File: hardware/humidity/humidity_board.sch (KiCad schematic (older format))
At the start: 11 parts

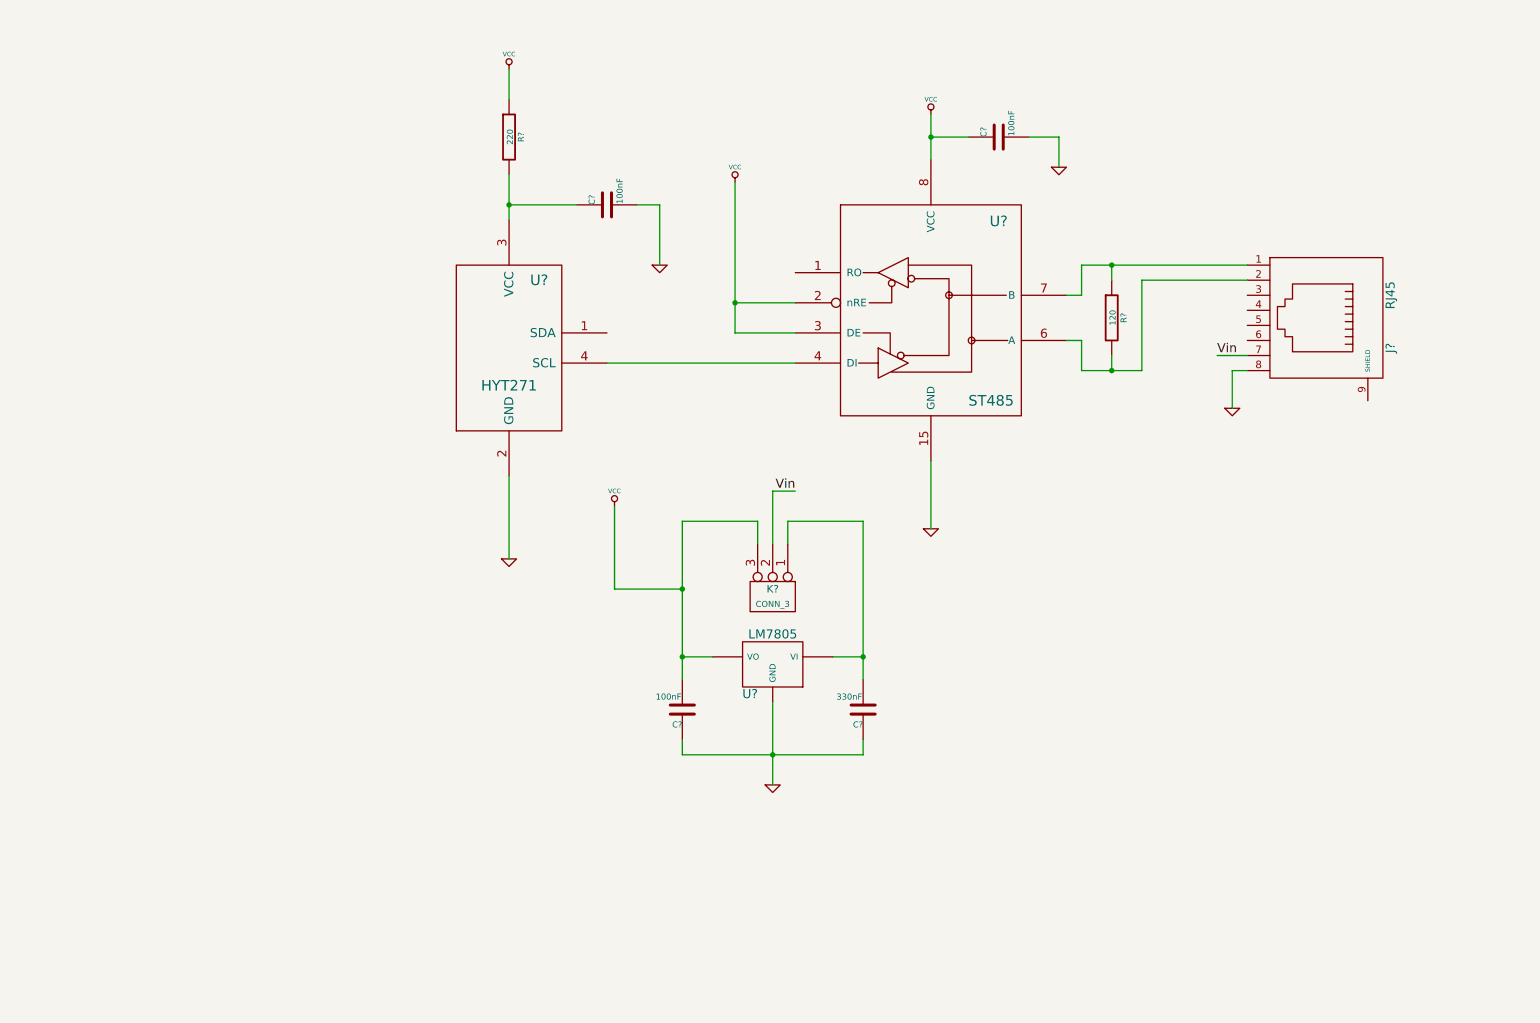
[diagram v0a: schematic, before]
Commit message: complete humidity board schematic
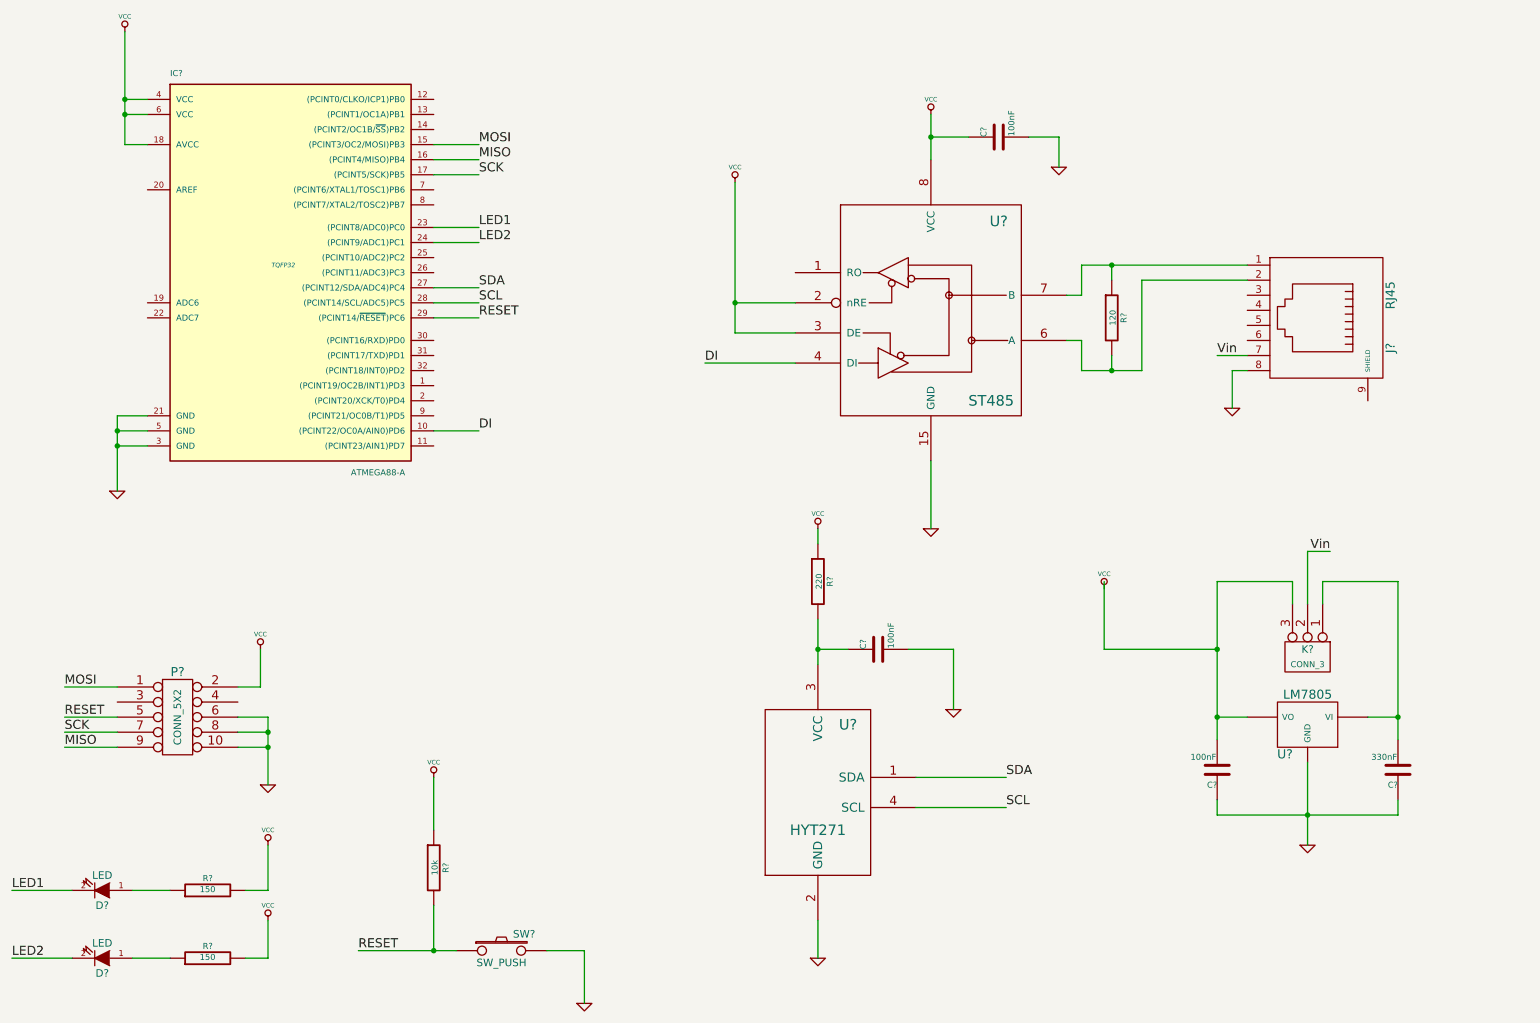
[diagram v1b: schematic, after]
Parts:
- added D? (x2): LED, ~, symbol LED
- added IC?: ATMEGA88-A, TQFP32, symbol ATMEGA88-A
- added P?: CONN_5X2, ~, symbol CONN_5X2
- added R?: 10k, ~, symbol R
- added R? (x2): 150, ~, symbol R
- added SW?: SW_PUSH, ~, symbol SW_PUSH
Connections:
- net GND: now also IC?.21 (GND), IC?.3 (GND), IC?.5 (GND), P?.10, P?.6, P?.8, SW?.2
- net VCC: now also IC?.18 (AVCC), IC?.4 (VCC), IC?.6 (VCC), P?.2, R?.1, R?.2, R?.2; no longer C?.2, K?.3 (P3), U?.VO
- net DI: now reaches U?.4 (DI)
- net DI: now also IC?.10 ((PCINT22/OC0A/AIN0)PD6); no longer U?.4 (SCL)
- net SDA: now reaches U?.1 (SDA)
- net SDA: now also IC?.27 ((PCINT12/SDA/ADC4)PC4)
- new net: C?.2, K?.3 (P3), U?.VO
- new net: D?.1 (A), R?.1 (x2)
- new net LED1: D?.2 (K), IC?.23 ((PCINT8/ADC0)PC0)
- new net LED2: D?.2 (K), IC?.24 ((PCINT9/ADC1)PC1)
- new net MISO: IC?.16 ((PCINT4/MISO)PB4), P?.9
- new net MOSI: IC?.15 ((PCINT3/OC2/MOSI)PB3), P?.1
- new net RESET: IC?.29 ((PCINT14/~RESET~)PC6), P?.5, R?.2, SW?.1
- new net SCK: IC?.17 ((PCINT5/SCK)PB5), P?.7
- new net SCL: IC?.28 ((PCINT14/SCL/ADC5)PC5), U?.4 (SCL)
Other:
- moved on the sheet: C?, K?, R?, U?

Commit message: hardware + bestellungen
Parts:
- removed C?: 100nF, ~, symbol C
- removed C?: 330nF, ~, symbol C
- removed K?: CONN_3, ~, symbol CONN_3
- removed U?: LM7805, ~, symbol LM7805
- added C?: 100nF, ~, symbol C
- added R? (x2): 22k, ~, symbol R
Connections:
- net Vin is gone; now on net VCC: J?.7
- net GND: now also J?.9 (SHIELD), R?.2
- net VCC: now also R?.1
- net at J?.2, U?.6 (A): now also C?.1, R?.2; no longer R?.2
- net at J?.1, R?.1, U?.7 (B): now also R?.1
- new net: C?.2, R?.2
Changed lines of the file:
@@
 LIBS:TSic50xF
 LIBS:ST485
-LIBS:HYT271
 LIBS:humidity_board-cache
 EELAYER 27 0
@@
 Sheet 1 1
 Title ""
-Date "24 mar 2014"
+Date "12 apr 2014"
 Rev ""
 Comp ""
@@
 Comment4 ""
 $EndDescr
-$Comp
-L GND #PWR?
-U 1 1 532DBFDE
-P 9300 6400
-F 0 "#PWR?" H 9300 6400 30  0001 C CNN
-F 1 "GND" H 9300 6330 30  0001 C CNN
-F 2 "" H 9300 6400 60  0000 C CNN
-F 3 "" H 9300 6400 60  0000 C CNN
-	1    9300 6400
-	1    0    0    -1
-$EndComp
 $Comp
 L VCC #PWR?
@@
 $EndComp
 $Comp
-L LM7805 U?
-U 1 1 532DDDDB
-P 9300 5600
-F 0 "U?" H 9450 5404 60  0000 C CNN
-F 1 "LM7805" H 9300 5800 60  0000 C CNN
-F 2 "~" H 9300 5600 60  0000 C CNN
-F 3 "~" H 9300 5600 60  0000 C CNN
-	1    9300 5600
-	-1   0    0    -1
-$EndComp
-$Comp
 L GND #PWR?
 U 1 1 532DDE77
@@
 	1    8800 3500
 	1    0    0    -1
-$EndComp
-$Comp
-L CONN_3 K?
-U 1 1 532DDF17
-P 9300 5150
-F 0 "K?" V 9250 5150 50  0000 C CNN
-F 1 "CONN_3" V 9350 5150 40  0000 C CNN
-F 2 "~" H 9300 5150 60  0000 C CNN
-F 3 "~" H 9300 5150 60  0000 C CNN
-	1    9300 5150
-	0    1    1    0
-$EndComp
-Text Label 9450 4450 2    60   ~ 0
-Vin
-Text Label 8700 3150 0    60   ~ 0
-Vin
-$Comp
-L VCC #PWR?
-U 1 1 532DE001
-P 7950 4700
-F 0 "#PWR?" H 7950 4800 30  0001 C CNN
-F 1 "VCC" H 7950 4800 30  0000 C CNN
-F 2 "" H 7950 4700 60  0000 C CNN
-F 3 "" H 7950 4700 60  0000 C CNN
-	1    7950 4700
-	1    0    0    -1
-$EndComp
-$Comp
-L C C?
-U 1 1 532DE060
-P 8700 5900
-F 0 "C?" H 8700 6000 40  0000 L CNN
-F 1 "100nF" H 8706 5815 40  0000 L CNN
-F 2 "~" H 8738 5750 30  0000 C CNN
-F 3 "~" H 8700 5900 60  0000 C CNN
-	1    8700 5900
-	-1   0    0    1
-$EndComp
-$Comp
-L C C?
-U 1 1 532DE066
-P 9900 5900
-F 0 "C?" H 9900 6000 40  0000 L CNN
-F 1 "330nF" H 9906 5815 40  0000 L CNN
-F 2 "~" H 9938 5750 30  0000 C CNN
-F 3 "~" H 9900 5900 60  0000 C CNN
-	1    9900 5900
-	-1   0    0    1
 $EndComp
 $Comp
@@
 	7700 3050 7800 3050
 Wire Wire Line
-	7800 3050 7800 3250
-Wire Wire Line
-	7800 3250 8200 3250
-Wire Wire Line
-	8000 3250 8000 3150
+	7800 3050 7800 3800
 Wire Wire Line
 	7800 2750 7800 2550
@@
 	8800 3250 8800 3500
 Wire Wire Line
-	9400 4800 9400 4650
-Wire Wire Line
-	9400 4650 9900 4650
-Wire Wire Line
-	9900 4650 9900 5700
-Wire Wire Line
-	9900 5550 9700 5550
-Wire Wire Line
-	9200 4800 9200 4650
-Wire Wire Line
-	9200 4650 8700 4650
-Wire Wire Line
-	8700 4650 8700 5700
-Wire Wire Line
-	8700 5550 8900 5550
-Wire Wire Line
-	9300 4800 9300 4450
-Wire Wire Line
-	9300 4450 9450 4450
-Wire Wire Line
 	8700 3150 8900 3150
-Connection ~ 8700 5100
-Wire Wire Line
-	9300 5850 9300 6400
-Connection ~ 8700 5550
-Connection ~ 9900 5550
-Wire Wire Line
-	8700 6100 8700 6200
-Wire Wire Line
-	8700 6200 9900 6200
-Connection ~ 9300 6200
-Wire Wire Line
-	9900 6200 9900 6100
 Connection ~ 8000 2550
 Wire Wire Line
 	8900 2650 8200 2650
 Wire Wire Line
-	8200 2650 8200 3250
-Connection ~ 8000 3250
+	8200 2650 8200 3800
 Wire Wire Line
 	6050 4900 6050 5200
 Wire Wire Line
 	6050 7150 6050 6900
-Wire Wire Line
-	7950 4650 7950 5100
-Wire Wire Line
-	7950 5100 8700 5100
 Wire Wire Line
 	1600 3550 1400 3550
@@
 Wire Wire Line
 	1750 7150 1500 7150
+$Comp
+L VCC #PWR?
+U 1 1 53493890
+P 8700 2950
+F 0 "#PWR?" H 8700 3050 30  0001 C CNN
+F 1 "VCC" H 8700 3050 30  0000 C CNN
+F 2 "" H 8700 2950 60  0000 C CNN
+F 3 "" H 8700 2950 60  0000 C CNN
+	1    8700 2950
+	1    0    0    -1
+$EndComp
+Wire Wire Line
+	8700 2950 8700 3150
+$Comp
+L C C?
+U 1 1 534938E9
+P 8000 3500
+F 0 "C?" H 8000 3600 40  0000 L CNN
+F 1 "100nF" H 8006 3415 40  0000 L CNN
+F 2 "~" H 8038 3350 30  0000 C CNN
+F 3 "~" H 8000 3500 60  0000 C CNN
+	1    8000 3500
+	-1   0    0    1
+$EndComp
+Wire Wire Line
+	8200 3800 7800 3800
+Wire Wire Line
+	8000 3700 8000 3800
+Connection ~ 8000 3800
+Wire Wire Line
+	8000 3150 8000 3300
+$Comp
+L R R?
+U 1 1 534939E7
+P 8350 2000
+F 0 "R?" V 8430 2000 40  0000 C CNN
+F 1 "22k" V 8357 2001 40  0000 C CNN
+F 2 "~" V 8280 2000 30  0000 C CNN
+F 3 "~" H 8350 2000 30  0000 C CNN
+	1    8350 2000
+	1    0    0    -1
+$EndComp
+$Comp
+L R R?
+U 1 1 534939ED
+P 8500 3050
+F 0 "R?" V 8580 3050 40  0000 C CNN
+F 1 "22k" V 8507 3051 40  0000 C CNN
+F 2 "~" V 8430 3050 30  0000 C CNN
+F 3 "~" H 8500 3050 30  0000 C CNN
+	1    8500 3050
+	1    0    0    -1
+$EndComp
+$Comp
+L GND #PWR?
+U 1 1 534939F3
+P 8500 3500
+F 0 "#PWR?" H 8500 3500 30  0001 C CNN
+F 1 "GND" H 8500 3430 30  0001 C CNN
+F 2 "" H 8500 3500 60  0000 C CNN
+F 3 "" H 8500 3500 60  0000 C CNN
+	1    8500 3500
+	1    0    0    -1
+$EndComp
+$Comp
+L VCC #PWR?
+U 1 1 534939F9
+P 8350 1600
+F 0 "#PWR?" H 8350 1700 30  0001 C CNN
+F 1 "VCC" H 8350 1700 30  0000 C CNN
+F 2 "" H 8350 1600 60  0000 C CNN
+F 3 "" H 8350 1600 60  0000 C CNN
+	1    8350 1600
+	1    0    0    -1
+$EndComp
+Wire Wire Line
+	8350 1600 8350 1750
+Wire Wire Line
+	8350 2250 8350 2650
+Connection ~ 8350 2650
+Wire Wire Line
+	8500 2800 8500 2550
+Connection ~ 8500 2550
+Wire Wire Line
+	8500 3300 8500 3500
+$Comp
+L GND #PWR?
+U 1 1 53493BBC
+P 9700 3600
+F 0 "#PWR?" H 9700 3600 30  0001 C CNN
+F 1 "GND" H 9700 3530 30  0001 C CNN
+F 2 "" H 9700 3600 60  0000 C CNN
+F 3 "" H 9700 3600 60  0000 C CNN
+	1    9700 3600
+	1    0    0    -1
+$EndComp
+Wire Wire Line
+	9700 3450 9700 3600
 $EndSCHEMATC

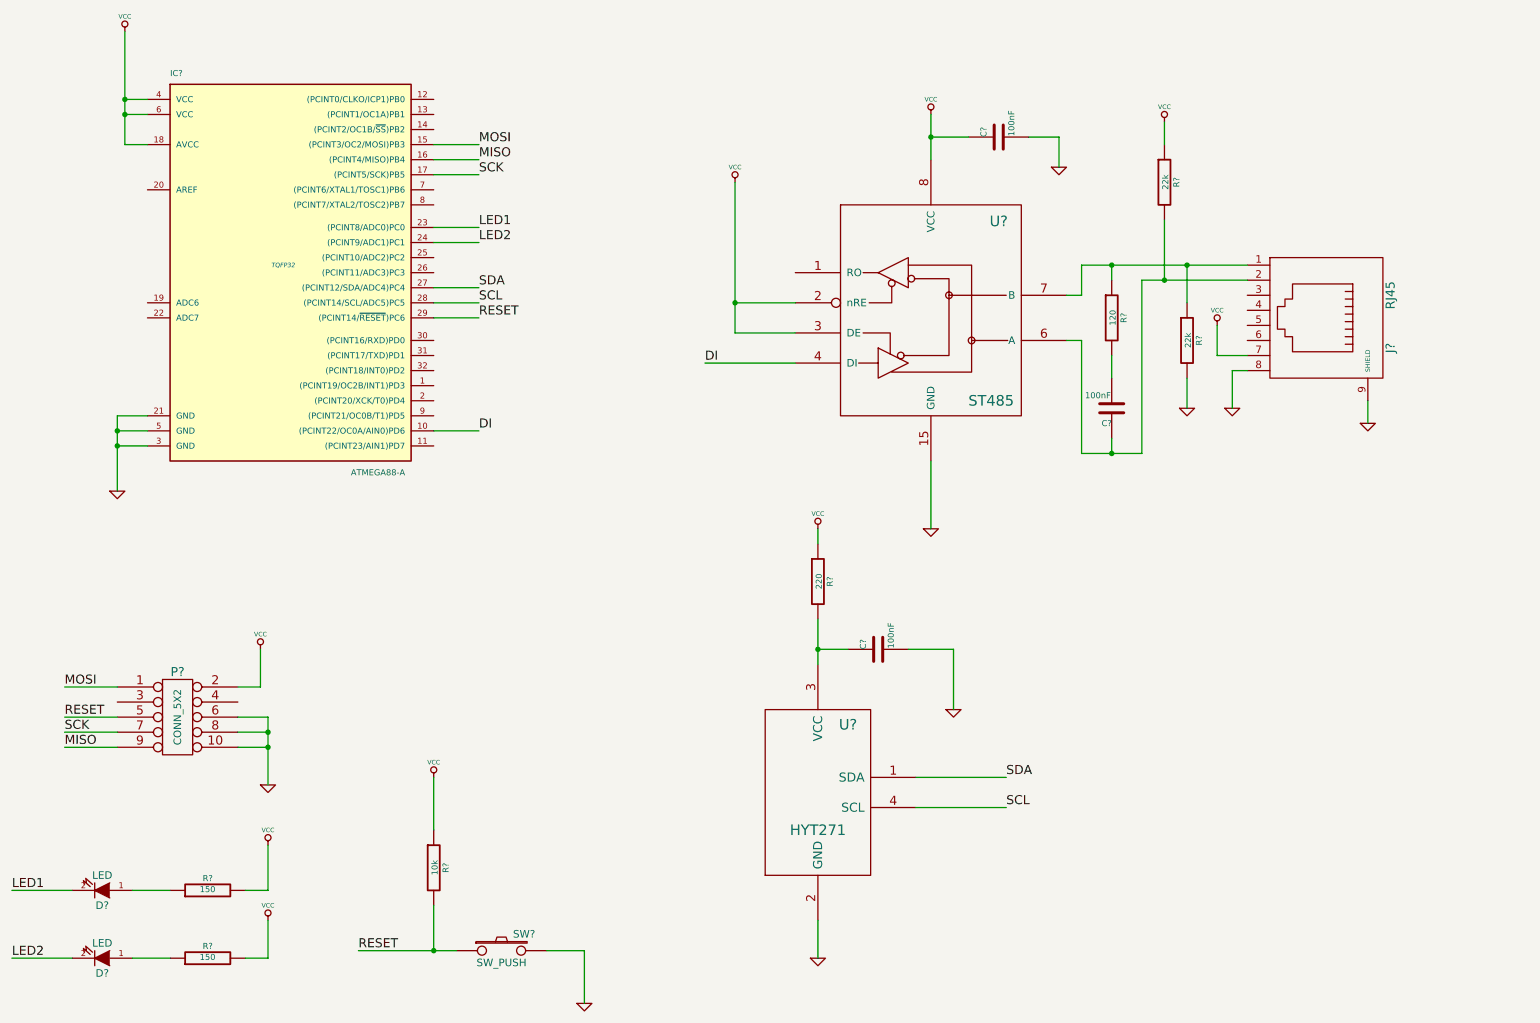
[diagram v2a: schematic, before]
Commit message: modify sensor board schematik
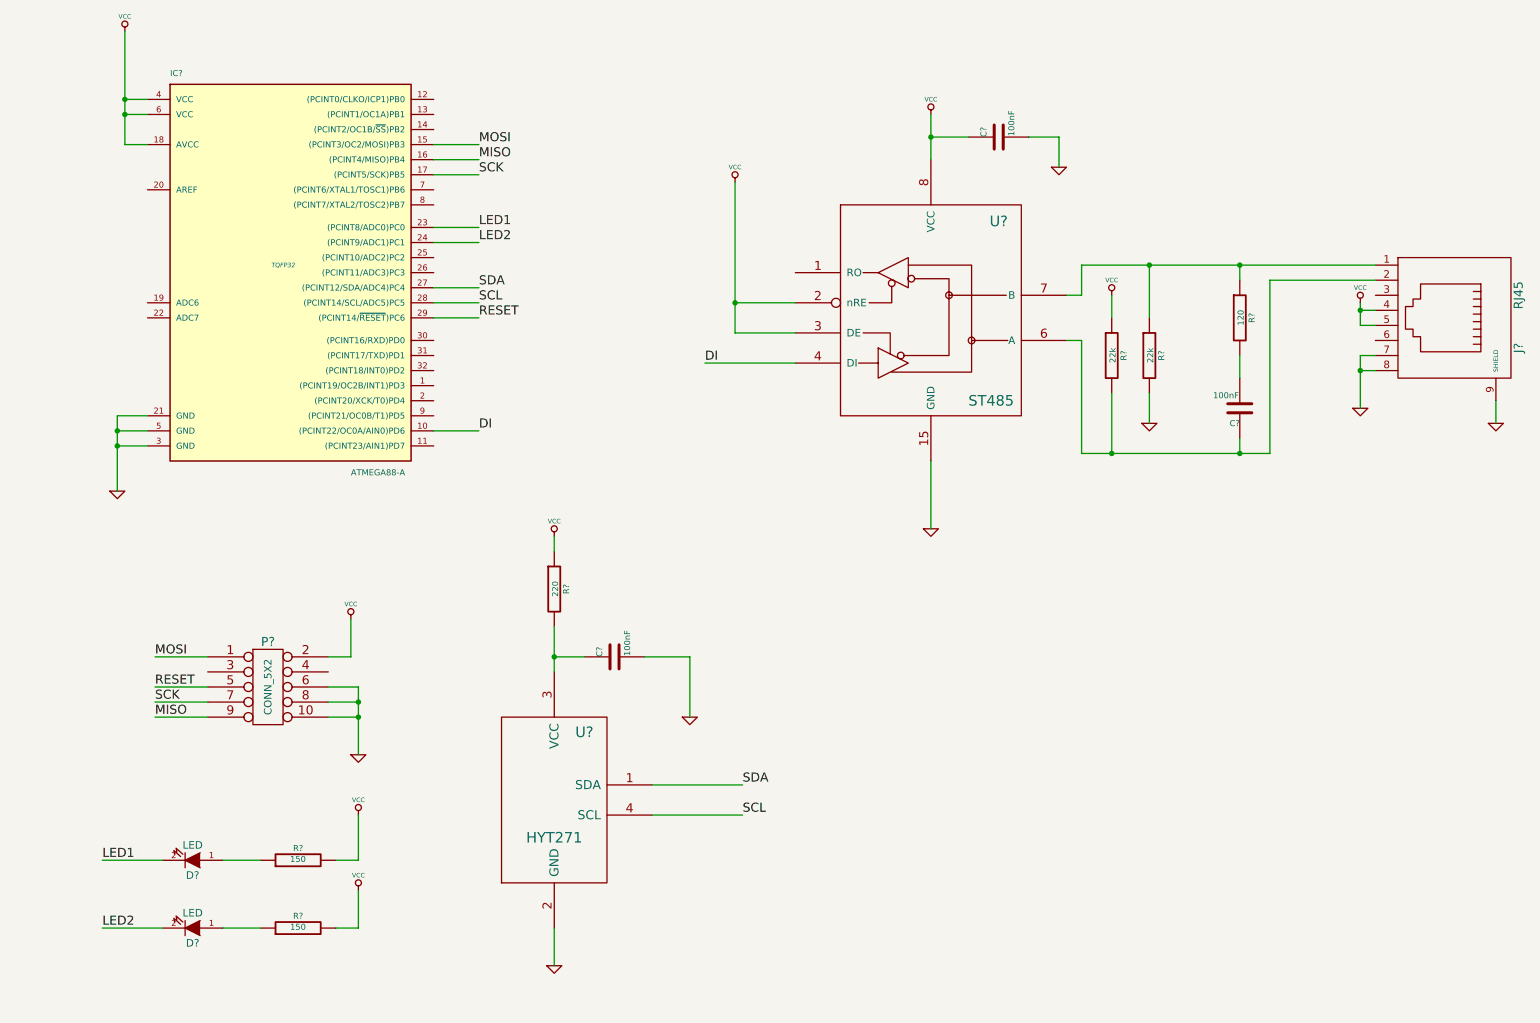
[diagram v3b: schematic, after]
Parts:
- removed R?: 10k, ~, symbol R
- removed R? (x2): 22k, ~, symbol R
- removed SW?: SW_PUSH, ~, symbol SW_PUSH
- added R? (x2): 22k, ~, symbol R
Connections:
- net GND: now also J?.7, R?.2
- net VCC: now also J?.4, J?.5, R?.1; no longer J?.7
- net at C?.1, J?.2, U?.6 (A): now also R?.2
- net at J?.1, R?.1, U?.7 (B): now also R?.1
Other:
- moved on the sheet: C?, D?, J?, P?, R?, U?
